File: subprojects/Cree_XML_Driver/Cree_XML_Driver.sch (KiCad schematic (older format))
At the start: 58 parts, among them J101 PJ-102AH, J102 Conn_01x03, Q101 Si2302CDS-T1, Q102 Si2302CDS-T1, Q103 Si2302CDS-T1, Q104 Si2302CDS-T1, U101 PAM2804, U102 PAM2804, U103 PAM2804, U104 PAM2804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

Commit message: Led horiz
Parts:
- TP101: footprint TestPoint:TestPoint_THTPad_2.0x2.0mm_Drill1.0mm -> TestPoint:TestPoint_THTPad_1.0x1.0mm_Drill0.5mm
- U105, U107: footprint Package_SO:SO-8_3.9x4.9mm_P1.27mm -> Package_SO:SOIC-8_3.9x4.9mm_P1.27mm

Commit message: Finish up led
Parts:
- added JP101, JP102, JP103, JP104: SolderJumper_3_Bridged12, Jumper:SolderJumper-3_P1.3mm_Bridged12_Pad1.0x1.5mm, symbol Jumper:SolderJumper_3_Bridged12
- J102: footprint Connector_PinSocket_1.27mm:PinSocket_1x03_P1.27mm_Vertical -> Connector_PinHeader_2.54mm:PinHeader_1x03_P2.54mm_Horizontal
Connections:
- net PWM_BB: now also JP103.2 (C); no longer R109.2, R110.2, U106.10 (5Y)
- net PWM_BW: now also JP104.2 (C); no longer U106.12 (6Y)
- new net: JP101.1 (A), JP102.1 (A), JP103.1 (A), JP104.3 (B), U106.10 (5Y)
- new net: JP101.3 (B), JP102.3 (B), JP103.3 (B), JP104.1 (A), U106.12 (6Y)
- new net PWM_BG: JP102.2 (C), R109.2
- new net PWM_BR: JP101.2 (C), R110.2
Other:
- note added: "RGB + W High Power Modes"
- moved on the sheet: C109, C110, C111, R113, R114, R115, R116, R117, R118, R119, R120, R121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

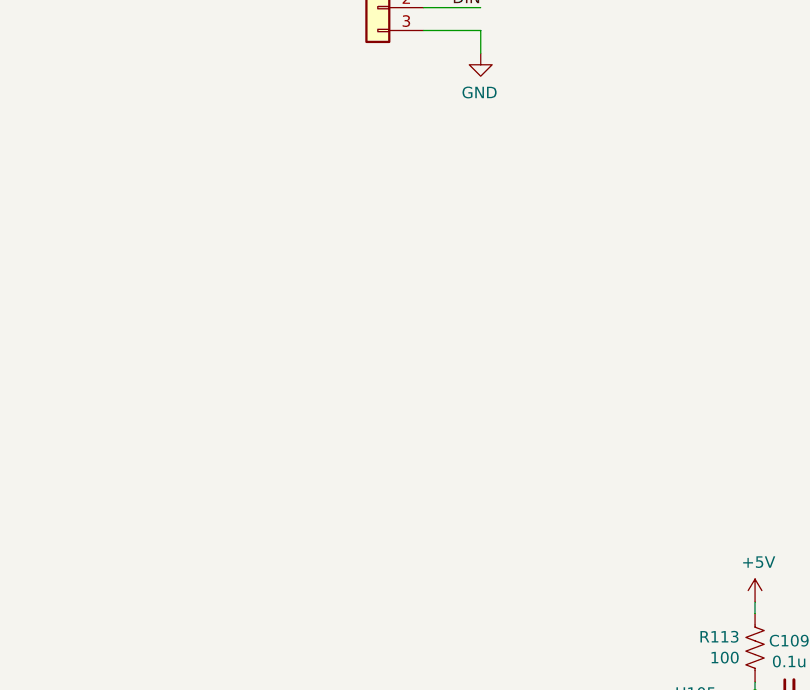
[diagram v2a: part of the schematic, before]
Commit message: Add JST cable for easier integration
Carries power, data and ground over a JST 1.25mm
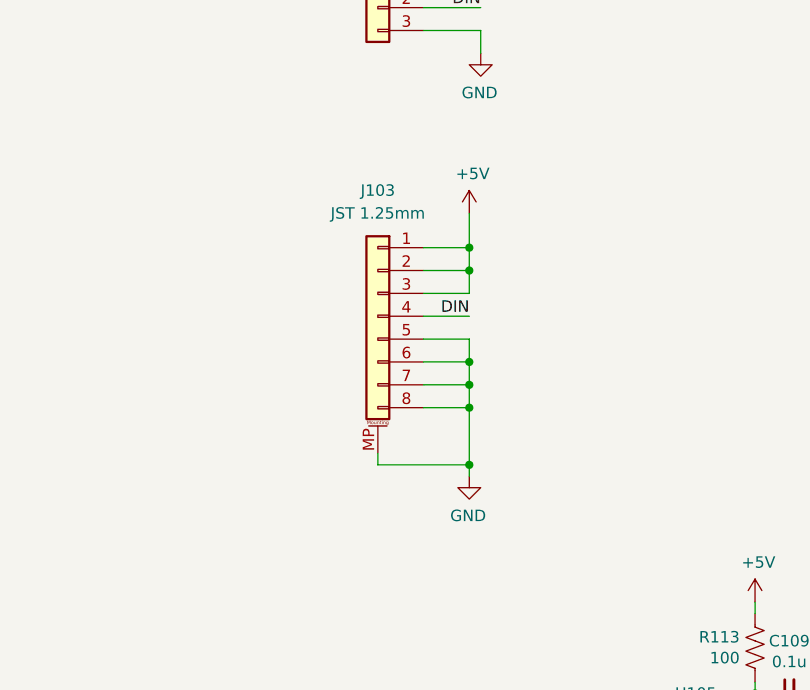
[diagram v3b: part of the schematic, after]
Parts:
- added J103: JST 1.25mm, Connector_Molex:Molex_PicoBlade_53261-0871_1x08-1MP_P1.25mm_Horizontal, symbol Connector_Generic_MountingPin:Conn_01x08_MountingPin
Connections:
- net +5V: now also J103.1 (Pin_1), J103.2 (Pin_2), J103.3 (Pin_3)
- net DIN: now also J103.4 (Pin_4)
- net GND: now also J103.5 (Pin_5), J103.6 (Pin_6), J103.7 (Pin_7), J103.8 (Pin_8), J103.MP (MountPin)
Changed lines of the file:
@@
 Text Notes 6150 6100 0    50   ~ 0
 RGB + W High Power Modes
+$Comp
+L power:+5V #PWR0147
+U 1 1 5FBAF2C8
+P 1150 3150
+F 0 "#PWR0147" H 1150 3000 50  0001 C CNN
+F 1 "+5V" H 1165 3323 50  0000 C CNN
+F 2 "" H 1150 3150 50  0001 C CNN
+F 3 "" H 1150 3150 50  0001 C CNN
+	1    1150 3150
+	1    0    0    -1
+$EndComp
+Wire Wire Line
+	950  3300 1150 3300
+Wire Wire Line
+	1150 3300 1150 3150
+Wire Wire Line
+	950  3400 1150 3400
+Wire Wire Line
+	1150 3400 1150 3300
+Connection ~ 1150 3300
+Wire Wire Line
+	950  3500 1150 3500
+Wire Wire Line
+	1150 3500 1150 3400
+Connection ~ 1150 3400
+Wire Wire Line
+	950  3600 1150 3600
+Text Label 1150 3600 2    50   ~ 0
+DIN
+$Comp
+L power:GND #PWR0148
+U 1 1 5FBE35DC
+P 1150 4300
+F 0 "#PWR0148" H 1150 4050 50  0001 C CNN
+F 1 "GND" H 1155 4127 50  0000 C CNN
+F 2 "" H 1150 4300 50  0001 C CNN
+F 3 "" H 1150 4300 50  0001 C CNN
+	1    1150 4300
+	-1   0    0    -1
+$EndComp
+Wire Wire Line
+	950  4000 1150 4000
+Wire Wire Line
+	1150 4000 1150 4250
+Wire Wire Line
+	950  3900 1150 3900
+Wire Wire Line
+	1150 3900 1150 4000
+Connection ~ 1150 4000
+Wire Wire Line
+	950  3800 1150 3800
+Wire Wire Line
+	1150 3800 1150 3900
+Connection ~ 1150 3900
+Wire Wire Line
+	950  3700 1150 3700
+Wire Wire Line
+	1150 3700 1150 3800
+Connection ~ 1150 3800
+Wire Wire Line
+	750  4200 750  4250
+Wire Wire Line
+	750  4250 1150 4250
+Connection ~ 1150 4250
+Wire Wire Line
+	1150 4250 1150 4300
+$Comp
+L Connector_Generic_MountingPin:Conn_01x08_MountingPin J103
+U 1 1 5FBAD9A9
+P 750 3600
+F 0 "J103" H 750 4150 50  0000 C CNN
+F 1 "JST 1.25mm" H 750 4050 50  0000 C CNN
+F 2 "Connector_Molex:Molex_PicoBlade_53261-0871_1x08-1MP_P1.25mm_Horizontal" H 750 3600 50  0001 C CNN
+F 3 "~" H 750 3600 50  0001 C CNN
+F 4 "0532610871" H 750 3600 50  0001 C CNN "MPN"
+F 5 "WM7626CT-ND" H 750 3600 50  0001 C CNN "Digikey"
+F 6 "1.25mm JST-like" H 750 3600 50  0001 C CNN "Note"
+	1    750  3600
+	-1   0    0    -1
+$EndComp
 $EndSCHEMATC

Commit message: BOM update and text cleanup
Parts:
- J101: LCSC (none) -> C84007
- J102: DNP (none) -> 1
- J103: LCSC (none) -> C29041; Note 1.25mm JST-like -> 1.25mm JST-like 01x08
- R109, R110, R111, R112, R113, R118: LCSC (none) -> C105588
- R114, R115, R116, R119, R120, R121: LCSC (none) -> C14675
- R117, R122: LCSC (none) -> C108661
- U106: LCSC C5605 -> C5605
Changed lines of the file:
@@
 F 4 "311-100KHRCT-ND" H 3000 5200 50  0001 C CNN "Digikey"
 F 5 "RC0603FR-07100KL" H 3000 5200 50  0001 C CNN "MPN"
+F 6 "C14675" H 3000 5200 50  0001 C CNN "LCSC"
 	1    3000 5200
 	-1   0    0    1
@@
 F 4 "311-100HRCT-ND" H 2400 5050 50  0001 C CNN "Digikey"
 F 5 "RC0603FR-07100RL" H 2400 5050 50  0001 C CNN "MPN"
+F 6 "C105588" H 2400 5050 50  0001 C CNN "LCSC"
 	1    2400 5050
 	1    0    0    -1
@@
 F 4 "311-33.0HRCT-ND" H 1750 5550 50  0001 C CNN "Digikey"
 F 5 "RC0603FR-0733RL" H 1750 5550 50  0001 C CNN "MPN"
+F 6 "C108661" H 1750 5550 50  0001 C CNN "LCSC"
 	1    1750 5550
 	0    1    -1   0
@@
 F 4 "311-100HRCT-ND" H 2150 6500 50  0001 C CNN "Digikey"
 F 5 "RC0603FR-07100RL" H 2150 6500 50  0001 C CNN "MPN"
+F 6 "C105588" H 2150 6500 50  0001 C CNN "LCSC"
 	1    2150 6500
 	1    0    0    -1
@@
 F 4 "311-33.0HRCT-ND" H 1550 7000 50  0001 C CNN "Digikey"
 F 5 "RC0603FR-0733RL" H 1550 7000 50  0001 C CNN "MPN"
+F 6 "C108661" H 1550 7000 50  0001 C CNN "LCSC"
 	1    1550 7000
 	0    1    -1   0
@@
 F 4 "311-100KHRCT-ND" H 3350 5200 50  0001 C CNN "Digikey"
 F 5 "RC0603FR-07100KL" H 3350 5200 50  0001 C CNN "MPN"
+F 6 "C14675" H 3350 5200 50  0001 C CNN "LCSC"
 	1    3350 5200
 	-1   0    0    1
@@
 F 4 "311-100KHRCT-ND" H 3700 5200 50  0001 C CNN "Digikey"
 F 5 "RC0603FR-07100KL" H 3700 5200 50  0001 C CNN "MPN"
+F 6 "C14675" H 3700 5200 50  0001 C CNN "LCSC"
 	1    3700 5200
 	-1   0    0    1
@@
 F 4 "311-100KHRCT-ND" H 3000 6650 50  0001 C CNN "Digikey"
 F 5 "RC0603FR-07100KL" H 3000 6650 50  0001 C CNN "MPN"
+F 6 "C14675" H 3000 6650 50  0001 C CNN "LCSC"
 	1    3000 6650
 	-1   0    0    1
@@
 F 4 "311-100KHRCT-ND" H 3350 6650 50  0001 C CNN "Digikey"
 F 5 "RC0603FR-07100KL" H 3350 6650 50  0001 C CNN "MPN"
+F 6 "C14675" H 3350 6650 50  0001 C CNN "LCSC"
 	1    3350 6650
 	-1   0    0    1
@@
 F 4 "311-100KHRCT-ND" H 3700 6650 50  0001 C CNN "Digikey"
 F 5 "RC0603FR-07100KL" H 3700 6650 50  0001 C CNN "MPN"
+F 6 "C14675" H 3700 6650 50  0001 C CNN "LCSC"
 	1    3700 6650
 	-1   0    0    1
@@
 F 4 "IC INVERTER SCHMITT 6CH" H 4900 7500 60  0001 L CNN "Description"
 F 5 "Nexperia" H 4900 7600 60  0001 L CNN "Manufacturer"
-F 6 " C5605 " H 4700 6500 50  0001 C CNN "LCSC"
+F 6 "C5605 " H 4700 6500 50  0001 C CNN "LCSC"
 F 7 "1727-2783-1-ND" H 4700 6500 50  0001 C CNN "Digikey"
 F 8 "74HC14D,653" H 4700 6500 50  0001 C CNN "MPN"
@@
 F 4 "311-100HRCT-ND" H 3400 3950 50  0001 C CNN "Digikey"
 F 5 "RC0603FR-07100RL" H 3400 3950 50  0001 C CNN "MPN"
+F 6 "C105588" H 3400 3950 50  0001 C CNN "LCSC"
 	1    3400 3950
 	0    1    1    0
@@
 F 4 "311-100HRCT-ND" H 5800 3950 50  0001 C CNN "Digikey"
 F 5 "RC0603FR-07100RL" H 5800 3950 50  0001 C CNN "MPN"
+F 6 "C105588" H 5800 3950 50  0001 C CNN "LCSC"
 	1    5800 3950
 	0    -1   1    0
@@
 F 4 "311-100HRCT-ND" H 9300 3950 50  0001 C CNN "Digikey"
 F 5 "RC0603FR-07100RL" H 9300 3950 50  0001 C CNN "MPN"
+F 6 "C105588" H 9300 3950 50  0001 C CNN "LCSC"
 	1    9300 3950
 	0    -1   1    0
@@
 F 4 "311-100HRCT-ND" H 6900 3950 50  0001 C CNN "Digikey"
 F 5 "RC0603FR-07100RL" H 6900 3950 50  0001 C CNN "MPN"
+F 6 "C105588" H 6900 3950 50  0001 C CNN "LCSC"
 	1    6900 3950
 	0    1    1    0
@@
 F 5 "CP-102AH-ND" H 850 1200 50  0001 C CNN "Digikey"
 F 6 "CONN PWR JACK 2X5.5MM SOLDER" H 850 1200 50  0001 C CNN "Note"
+F 7 "C84007" H 850 1200 50  0001 C CNN "LCSC"
 	1    850  1200
 	1    0    0    -1
@@
 F 2 "Connector_PinHeader_2.54mm:PinHeader_1x03_P2.54mm_Horizontal" H 750 2250 50  0001 C CNN
 F 3 "~" H 750 2250 50  0001 C CNN
+F 4 "1" H 750 2250 50  0001 C CNN "DNP"
 	1    750  2250
 	-1   0    0    -1
@@
 F 4 "0532610871" H 750 3600 50  0001 C CNN "MPN"
 F 5 "WM7626CT-ND" H 750 3600 50  0001 C CNN "Digikey"
-F 6 "1.25mm JST-like" H 750 3600 50  0001 C CNN "Note"
+F 6 "1.25mm JST-like 01x08" H 750 3600 50  0001 C CNN "Note"
+F 7 "C29041" H 750 3600 50  0001 C CNN "LCSC"
 	1    750  3600
 	-1   0    0    -1

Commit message: Schematic field cleanup
Fixed rescue libs
Remove stray spaces
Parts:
- D101: symbol Cree_XML_Driver-rescue:LED_RGBW_EP-mylib -> mylib:LED_RGBW_EP
- L101, L102, L103, L104: Note 4.7uH ±20% 2A 60mΩ SMD,4x4x3mm -> 4.7uH ±20% 2A 60mΩ SMD,4x4x3mm
- LOGO101: symbol Cree_XML_Driver-rescue:MYLIB_CWW_COPPER-mylib -> mylib:MYLIB_CWW_COPPER
- U101, U102, U103, U104: symbol Cree_XML_Driver-rescue:PAM2804-mylib -> mylib:PAM2804; Manufacturer Diodes Incorporated -> Diodes Incorporated
- U105, U107: LCSC C114581 -> C114581
- U106: LCSC C5605 -> C5605
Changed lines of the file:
@@
 $EndDescr
 $Comp
-L Cree_XML_Driver-rescue:PAM2804-mylib U101
+L mylib:PAM2804 U101
 U 1 1 5F7BE2DE
 P 3850 950
@@
 F 3 "https://www.diodes.com/assets/Datasheets/PAM2804.pdf" H 3600 600 50  0001 C CNN
 F 4 "C71463" H 3850 950 50  0001 C CNN "LCSC"
-F 5 "Diodes Incorporated " H 3850 950 50  0001 C CNN "Manufacturer"
+F 5 "Diodes Incorporated" H 3850 950 50  0001 C CNN "Manufacturer"
 F 6 "PAM2804AAB010DICT-ND" H 3850 950 50  0001 C CNN "Digikey"
 F 7 "PAM2804AAB010" H 3850 950 50  0001 C CNN "MPN"
@@
 F 3 "~" H 4550 850 50  0001 C CNN
 F 4 "SLW4030S4R7MST" H 4550 850 50  0001 C CNN "MPN"
-F 5 "4.7uH ±20% 2A 60mΩ SMD,4x4x3mm " H 4550 850 50  0001 C CNN "Note"
+F 5 "4.7uH ±20% 2A 60mΩ SMD,4x4x3mm" H 4550 850 50  0001 C CNN "Note"
 F 6 "C206284, C15269" H 4550 850 50  0001 C CNN "LCSC"
 F 7 "587-5994-1-ND" H 4550 850 50  0001 C CNN "Digikey"
@@
 	10025 6450 10025 6500
 $Comp
-L Cree_XML_Driver-rescue:MYLIB_CWW_COPPER-mylib LOGO101
+L mylib:MYLIB_CWW_COPPER LOGO101
 U 1 1 5E6F1CB4
 P 6050 7850
@@
 SERCOM 0
 $Comp
-L Cree_XML_Driver-rescue:LED_RGBW_EP-mylib D101
+L mylib:LED_RGBW_EP D101
 U 1 1 5F8411AA
 P 6250 2450
@@
 $EndComp
 $Comp
-L Cree_XML_Driver-rescue:PAM2804-mylib U103
+L mylib:PAM2804 U103
 U 1 1 5F8ADF81
 P 3850 2300
@@
 F 3 "https://www.diodes.com/assets/Datasheets/PAM2804.pdf" H 3600 1950 50  0001 C CNN
 F 4 "C71463" H 3850 2300 50  0001 C CNN "LCSC"
-F 5 "Diodes Incorporated " H 3850 2300 50  0001 C CNN "Manufacturer"
+F 5 "Diodes Incorporated" H 3850 2300 50  0001 C CNN "Manufacturer"
 F 6 "PAM2804AAB010DICT-ND" H 3850 2300 50  0001 C CNN "Digikey"
 F 7 "PAM2804AAB010" H 3850 2300 50  0001 C CNN "MPN"
@@
 F 3 "~" H 4550 2200 50  0001 C CNN
 F 4 "SLW4030S4R7MST" H 4550 2200 50  0001 C CNN "MPN"
-F 5 "4.7uH ±20% 2A 60mΩ SMD,4x4x3mm " H 4550 2200 50  0001 C CNN "Note"
+F 5 "4.7uH ±20% 2A 60mΩ SMD,4x4x3mm" H 4550 2200 50  0001 C CNN "Note"
 F 6 "C206284, C15269" H 4550 2200 50  0001 C CNN "LCSC"
 F 7 "587-5994-1-ND" H 4550 2200 50  0001 C CNN "Digikey"
@@
 	5350 850  6050 850
 $Comp
-L Cree_XML_Driver-rescue:PAM2804-mylib U102
+L mylib:PAM2804 U102
 U 1 1 5FAA20E8
 P 8850 950
@@
 F 3 "https://www.diodes.com/assets/Datasheets/PAM2804.pdf" H 8600 600 50  0001 C CNN
 F 4 "C71463" H 8850 950 50  0001 C CNN "LCSC"
-F 5 "Diodes Incorporated " H 8850 950 50  0001 C CNN "Manufacturer"
+F 5 "Diodes Incorporated" H 8850 950 50  0001 C CNN "Manufacturer"
 F 6 "PAM2804AAB010DICT-ND" H 8850 950 50  0001 C CNN "Digikey"
 F 7 "PAM2804AAB010" H 8850 950 50  0001 C CNN "MPN"
@@
 F 3 "~" H 8150 850 50  0001 C CNN
 F 4 "SLW4030S4R7MST" H 8150 850 50  0001 C CNN "MPN"
-F 5 "4.7uH ±20% 2A 60mΩ SMD,4x4x3mm " H 8150 850 50  0001 C CNN "Note"
+F 5 "4.7uH ±20% 2A 60mΩ SMD,4x4x3mm" H 8150 850 50  0001 C CNN "Note"
 F 6 "C206284, C15269" H 8150 850 50  0001 C CNN "LCSC"
 F 7 "587-5994-1-ND" H 8150 850 50  0001 C CNN "Digikey"
@@
 PWM_W
 $Comp
-L Cree_XML_Driver-rescue:PAM2804-mylib U104
+L mylib:PAM2804 U104
 U 1 1 5FAA2114
 P 8850 2300
@@
 F 3 "https://www.diodes.com/assets/Datasheets/PAM2804.pdf" H 8600 1950 50  0001 C CNN
 F 4 "C71463" H 8850 2300 50  0001 C CNN "LCSC"
-F 5 "Diodes Incorporated " H 8850 2300 50  0001 C CNN "Manufacturer"
+F 5 "Diodes Incorporated" H 8850 2300 50  0001 C CNN "Manufacturer"
 F 6 "PAM2804AAB010DICT-ND" H 8850 2300 50  0001 C CNN "Digikey"
 F 7 "PAM2804AAB010" H 8850 2300 50  0001 C CNN "MPN"
@@
 F 3 "~" H 8150 2200 50  0001 C CNN
 F 4 "SLW4030S4R7MST" H 8150 2200 50  0001 C CNN "MPN"
-F 5 "4.7uH ±20% 2A 60mΩ SMD,4x4x3mm " H 8150 2200 50  0001 C CNN "Note"
+F 5 "4.7uH ±20% 2A 60mΩ SMD,4x4x3mm" H 8150 2200 50  0001 C CNN "Note"
 F 6 "C206284, C15269" H 8150 2200 50  0001 C CNN "LCSC"
 F 7 "587-5994-1-ND" H 8150 2200 50  0001 C CNN "Digikey"
@@
 F 4 "IC INVERTER SCHMITT 6CH" H 4900 7500 60  0001 L CNN "Description"
 F 5 "Nexperia" H 4900 7600 60  0001 L CNN "Manufacturer"
-F 6 "C5605 " H 4700 6500 50  0001 C CNN "LCSC"
+F 6 "C5605" H 4700 6500 50  0001 C CNN "LCSC"
 F 7 "1727-2783-1-ND" H 4700 6500 50  0001 C CNN "Digikey"
 F 8 "74HC14D,653" H 4700 6500 50  0001 C CNN "MPN"
@@
 F 2 "Package_SO:SOIC-8_3.9x4.9mm_P1.27mm" H 1850 7250 50  0001 C CNN
 F 3 "https://cdn-shop.adafruit.com/datasheets/WS2811.pdf" H 1950 7350 50  0001 C CNN
-F 4 "C114581 " H 2150 7100 50  0001 C CNN "LCSC"
+F 4 "C114581" H 2150 7100 50  0001 C CNN "LCSC"
 F 5 "Worldsemi" H 2150 7100 50  0001 C CNN "Manufacturer"
 	1    2150 7100
@@
 F 2 "Package_SO:SOIC-8_3.9x4.9mm_P1.27mm" H 2100 5800 50  0001 C CNN
 F 3 "https://cdn-shop.adafruit.com/datasheets/WS2811.pdf" H 2200 5900 50  0001 C CNN
-F 4 "C114581 " H 2400 5650 50  0001 C CNN "LCSC"
+F 4 "C114581" H 2400 5650 50  0001 C CNN "LCSC"
 F 5 "Worldsemi" H 2400 5650 50  0001 C CNN "Manufacturer"
 	1    2400 5650
